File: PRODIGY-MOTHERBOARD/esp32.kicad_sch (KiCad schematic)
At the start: 14 parts, among them J15 Bus_M.2_Socket_B, J16 USB_C_Receptacle, J17 Conn_02x20_Odd_Even, SW2 SW_Push

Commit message: Finished v0.1 schematic.
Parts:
- added FID10, FID9: Fiducial, symbol Mechanical:Fiducial
- J6: renamed from J16; footprint (none) -> Connector_USB:USB_C_Receptacle_G-Switch_GT-USB-7025
- renumbered C57 to C26, D34 to D10, D31 to D11, D32 to D12, D33 to D13, D35 to D9, J15 to J7, J17 to J8, R34 to R19, R35 to R20, R32 to R21, R33 to R22
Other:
- moved on the sheet: J8

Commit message: MBT Schematic improved
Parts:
- J8: footprint Connector_PinHeader_2.54mm:PinHeader_2x20_P2.54mm_Horizontal -> Connector_IDC:IDC-Header_2x20_P2.54mm_Horizontal
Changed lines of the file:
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@@
 			)
 		)
-		(property "Footprint" "Connector_PinHeader_2.54mm:PinHeader_2x20_P2.54mm_Horizontal"
+		(property "Footprint" "Connector_IDC:IDC-Header_2x20_P2.54mm_Horizontal"
 			(at 238.76 119.38 0)
 			(effects

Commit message: schematic v0.2 finalized
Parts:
- added H10: MountingHole, MountingHole:MountingHole_3.2mm_M3_ISO7380_Pad_TopBottom, symbol Mechanical:MountingHole
- J8: now not fitted; now left out of the parts list
- renumbered C26 to C25
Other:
- note added: "In USB CDC Mode BOOT button is not needed"
- note removed: "In USB CDC Mode BOOT button is not needed, But externally accessible"
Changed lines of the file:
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@@
 		)
 	)
-	(text "In USB CDC Mode\nBOOT button is not needed,\nBut externally accessible"
+	(text "In USB CDC Mode\nBOOT button is not needed"
 		(exclude_from_sim no)
 		(at 109.22 190.754 0)
@@
 		(dnp no)
 		(fields_autoplaced yes)
-		(property "Reference" "#PWR052"
+		(property "Reference" "#PWR055"
 			(at 158.75 31.75 0)
 			(effects
@@
 			(project "PRODIGY-MOTHERBOARD"
 				(path "/f1c25860-8989-4190-bd24-2491d23ca7d9/4747deee-8806-443e-847a-65f550cadde4"
-					(reference "#PWR052")
+					(reference "#PWR055")
 					(unit 1)
 				)
@@
 		(dnp no)
 		(fields_autoplaced yes)
-		(property "Reference" "#PWR047"
+		(property "Reference" "#PWR050"
 			(at 44.45 189.23 0)
 			(effects
@@
 			(project "PRODIGY-MOTHERBOARD"
 				(path "/f1c25860-8989-4190-bd24-2491d23ca7d9/4747deee-8806-443e-847a-65f550cadde4"
-					(reference "#PWR047")
+					(reference "#PWR050")
 					(unit 1)
 				)
@@
 		(dnp no)
 		(fields_autoplaced yes)
-		(property "Reference" "#PWR054"
+		(property "Reference" "#PWR057"
 			(at 223.52 97.79 0)
 			(effects
@@
 			(project "PRODIGY-MOTHERBOARD"
 				(path "/f1c25860-8989-4190-bd24-2491d23ca7d9/4747deee-8806-443e-847a-65f550cadde4"
-					(reference "#PWR054")
+					(reference "#PWR057")
 					(unit 1)
 				)
@@
 		(dnp no)
 		(fields_autoplaced yes)
-		(property "Reference" "#PWR045"
+		(property "Reference" "#PWR048"
 			(at 38.1 157.48 0)
 			(effects
@@
 			(project "PRODIGY-MOTHERBOARD"
 				(path "/f1c25860-8989-4190-bd24-2491d23ca7d9/4747deee-8806-443e-847a-65f550cadde4"
-					(reference "#PWR045")
+					(reference "#PWR048")
 					(unit 1)
 				)
@@
 		(dnp no)
 		(fields_autoplaced yes)
-		(property "Reference" "C26"
+		(property "Reference" "C25"
 			(at 63.5 172.7199 0)
 			(effects
@@
 			(project "PRODIGY-MOTHERBOARD"
 				(path "/f1c25860-8989-4190-bd24-2491d23ca7d9/4747deee-8806-443e-847a-65f550cadde4"
-					(reference "C26")
+					(reference "C25")
 					(unit 1)
 				)
@@
 		(dnp no)
 		(fields_autoplaced yes)
-		(property "Reference" "#PWR049"
+		(property "Reference" "#PWR052"
 			(at 76.2 55.88 0)
 			(effects
@@
 			(project "PRODIGY-MOTHERBOARD"
 				(path "/f1c25860-8989-4190-bd24-2491d23ca7d9/4747deee-8806-443e-847a-65f550cadde4"
-					(reference "#PWR049")
+					(reference "#PWR052")
 					(unit 1)
 				)
@@
 		(dnp no)
 		(fields_autoplaced yes)
-		(property "Reference" "#PWR050"
+		(property "Reference" "#PWR053"
 			(at 85.09 92.71 0)
 			(effects
@@
 			(project "PRODIGY-MOTHERBOARD"
 				(path "/f1c25860-8989-4190-bd24-2491d23ca7d9/4747deee-8806-443e-847a-65f550cadde4"
-					(reference "#PWR050")
+					(reference "#PWR053")
 					(unit 1)
 				)
@@
 		(dnp no)
 		(fields_autoplaced yes)
-		(property "Reference" "#PWR048"
+		(property "Reference" "#PWR051"
 			(at 63.5 129.54 0)
 			(effects
@@
 			(project "PRODIGY-MOTHERBOARD"
 				(path "/f1c25860-8989-4190-bd24-2491d23ca7d9/4747deee-8806-443e-847a-65f550cadde4"
-					(reference "#PWR048")
+					(reference "#PWR051")
 					(unit 1)
 				)
@@
 		(dnp no)
 		(fields_autoplaced yes)
-		(property "Reference" "#PWR046"
+		(property "Reference" "#PWR049"
 			(at 40.64 130.81 0)
 			(effects
@@
 			(project "PRODIGY-MOTHERBOARD"
 				(path "/f1c25860-8989-4190-bd24-2491d23ca7d9/4747deee-8806-443e-847a-65f550cadde4"
-					(reference "#PWR046")
+					(reference "#PWR049")
 					(unit 1)
 				)
@@
 	)
 	(symbol
-		(lib_id "Connector_Generic:Conn_02x20_Odd_Even")
-		(at 238.76 119.38 0)
+		(lib_id "Mechanical:MountingHole")
+		(at 246.38 38.1 0)
 		(unit 1)
 		(exclude_from_sim no)
@@
 		(on_board yes)
 		(dnp no)
+		(fields_autoplaced yes)
+		(property "Reference" "H10"
+			(at 248.92 37.465 0)
+			(effects
+				(font
+					(size 1.27 1.27)
+				)
+				(justify left)
+			)
+		)
+		(property "Value" "MountingHole"
+			(at 248.92 40.005 0)
+			(effects
+				(font
+					(size 1.27 1.27)
+				)
+				(justify left)
+				(hide yes)
+			)
+		)
+		(property "Footprint" "MountingHole:MountingHole_3.2mm_M3_ISO7380_Pad_TopBottom"
+			(at 246.38 38.1 0)
+			(effects
+				(font
+					(size 1.27 1.27)
+				)
+				(hide yes)
+			)
+		)
+		(property "Datasheet" "~"
+			(at 246.38 38.1 0)
+			(effects
+				(font
+					(size 1.27 1.27)
+				)
+				(hide yes)
+			)
+		)
+		(property "Description" ""
+			(at 246.38 38.1 0)
+			(effects
+				(font
+					(size 1.27 1.27)
+				)
+				(hide yes)
+			)
+		)
+		(property "JLCPCB" ""
+			(at 246.38 38.1 0)
+			(effects
+				(font
+					(size 1.27 1.27)
+				)
+				(hide yes)
+			)
+		)
+		(instances
+			(project "PRODIGY-MOTHERBOARD"
+				(path "/f1c25860-8989-4190-bd24-2491d23ca7d9/4747deee-8806-443e-847a-65f550cadde4"
+					(reference "H10")
+					(unit 1)
+				)
+			)
+		)
+	)
+	(symbol
+		(lib_id "Connector_Generic:Conn_02x20_Odd_Even")
+		(at 238.76 119.38 0)
+		(unit 1)
+		(exclude_from_sim yes)
+		(in_bom no)
+		(on_board no)
+		(dnp yes)
 		(fields_autoplaced yes)
 		(property "Reference" "J8"
@@
 		(dnp no)
 		(fields_autoplaced yes)
-		(property "Reference" "#PWR056"
+		(property "Reference" "#PWR059"
 			(at 255.27 97.79 0)
 			(effects
@@
 			(project "PRODIGY-MOTHERBOARD"
 				(path "/f1c25860-8989-4190-bd24-2491d23ca7d9/4747deee-8806-443e-847a-65f550cadde4"
-					(reference "#PWR056")
+					(reference "#PWR059")
 					(unit 1)
 				)
@@
 		(dnp no)
 		(fields_autoplaced yes)
-		(property "Reference" "#PWR055"
+		(property "Reference" "#PWR058"
 			(at 227.33 153.67 0)
 			(effects
@@
 			(project "PRODIGY-MOTHERBOARD"
 				(path "/f1c25860-8989-4190-bd24-2491d23ca7d9/4747deee-8806-443e-847a-65f550cadde4"
-					(reference "#PWR055")
+					(reference "#PWR058")
 					(unit 1)
 				)
@@
 		(dnp no)
 		(fields_autoplaced yes)
-		(property "Reference" "#PWR051"
+		(property "Reference" "#PWR054"
 			(at 90.17 92.71 0)
 			(effects
@@
 			(project "PRODIGY-MOTHERBOARD"
 				(path "/f1c25860-8989-4190-bd24-2491d23ca7d9/4747deee-8806-443e-847a-65f550cadde4"
-					(reference "#PWR051")
+					(reference "#PWR054")
 					(unit 1)
 				)
@@
 		(dnp no)
 		(fields_autoplaced yes)
-		(property "Reference" "#PWR053"
+		(property "Reference" "#PWR056"
 			(at 158.75 137.16 0)
 			(effects
@@
 			(project "PRODIGY-MOTHERBOARD"
 				(path "/f1c25860-8989-4190-bd24-2491d23ca7d9/4747deee-8806-443e-847a-65f550cadde4"
-					(reference "#PWR053")
-					(unit 1)
-				)
+					(reference "#PWR056")
+					(unit 1)
+				)

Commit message: ESP32 schematic complete.
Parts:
- H10: footprint MountingHole:MountingHole_3.2mm_M3_ISO7380_Pad_TopBottom -> MountingHole:MountingHole_4.3mm_M4_ISO14580_Pad
- J7: footprint (none) -> m.2_edge_connector_key_a:121992304
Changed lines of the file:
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@@
 			)
 		)
-		(property "Footprint" "MountingHole:MountingHole_3.2mm_M3_ISO7380_Pad_TopBottom"
+		(property "Footprint" "MountingHole:MountingHole_4.3mm_M4_ISO14580_Pad"
 			(at 246.38 38.1 0)
 			(effects
@@
 			)
 		)
-		(property "Footprint" ""
+		(property "Footprint" "m.2_edge_connector_key_a:121992304"
 			(at 158.75 53.34 0)
 			(effects

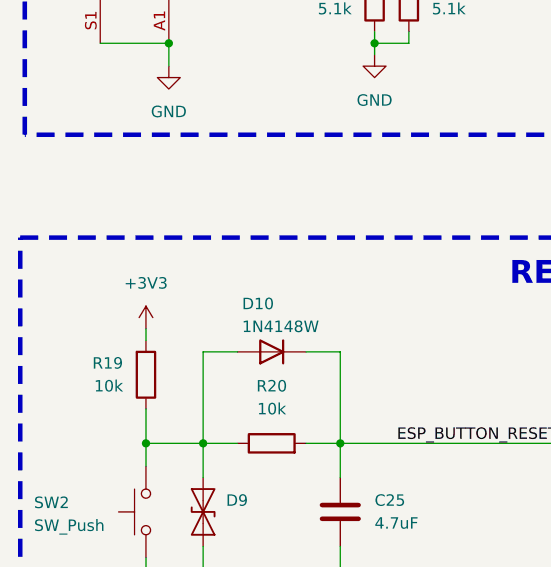
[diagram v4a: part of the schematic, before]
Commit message: Motherboard footprints assigned.
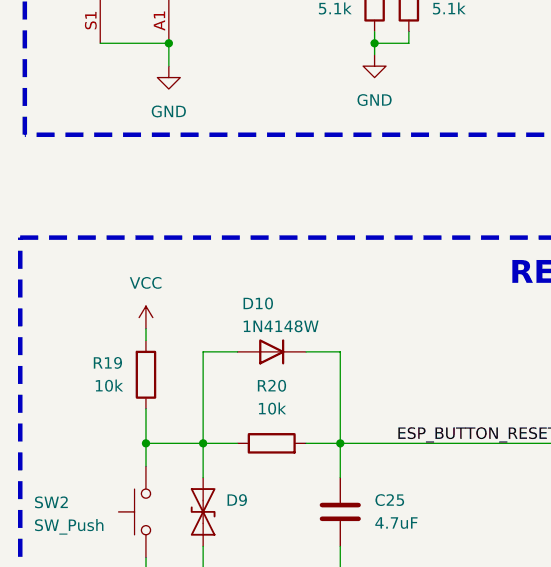
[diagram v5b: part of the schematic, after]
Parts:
- C25: footprint (none) -> Capacitor_SMD:C_0805_2012Metric
- FID10, FID9: footprint (none) -> Fiducial:Fiducial_1mm_Mask3mm
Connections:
- net +3V3: no longer R19.2
- new net VCC: R19.2

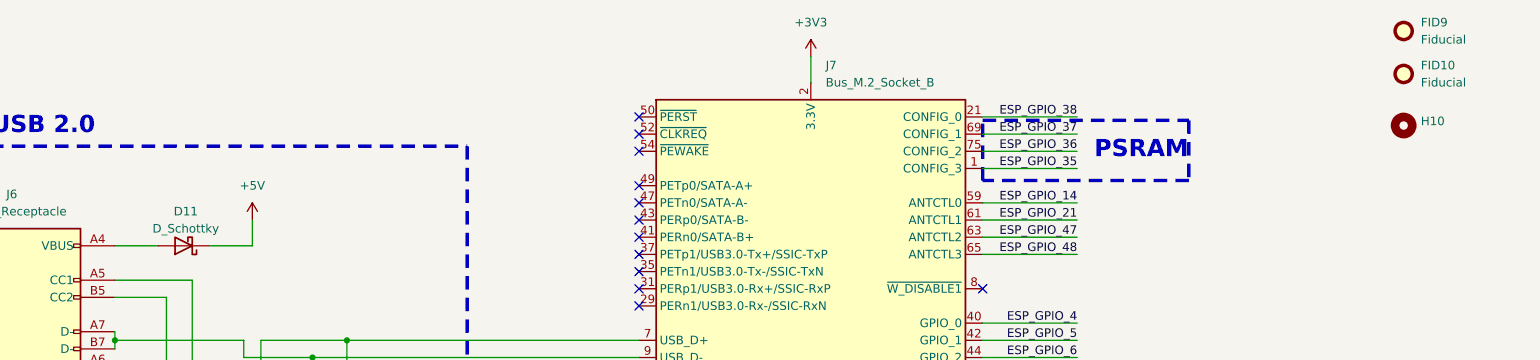
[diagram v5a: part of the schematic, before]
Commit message: finished motherboard bom and updated footprints
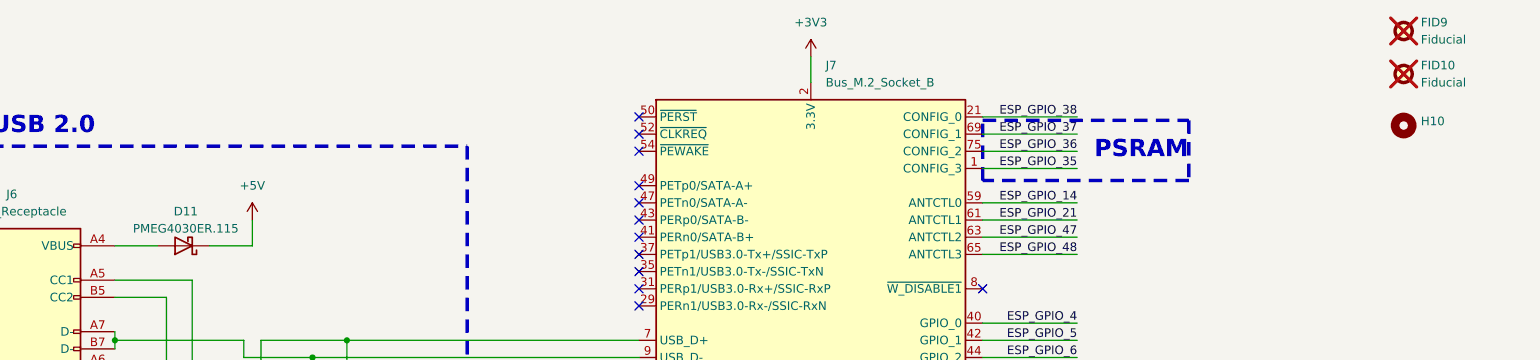
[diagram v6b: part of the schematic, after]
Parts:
- C25: TME (none) -> CL21A475KAQNNNG
- D10: footprint Diode_SMD:D_SOD-123 -> Diode_SMD:D_SOD-323; TME (none) -> 1N4148WSTR-SMC
- D11: value D_Schottky -> PMEG4030ER.115; footprint Diode_SMD:D_SMB -> Diode_SMD:Nexperia_CFP3_SOD-123W; TME (none) -> PMEG4030ER.115
- D12, D13, D9: TME (none) -> SD05.TCT
- FID10, FID9: now not fitted
- H10: MOUSER (none) -> 710-9774040360R
- J6: MOUSER (none) -> 523-GSB1C411111DS1HR
- J7: TME (none) -> 123A-58B00
- R19, R20: TME (none) -> WR06X1002FTL
- R21, R22: TME (none) -> AC0603FR-075K1L
- SW2: TME (none) -> KMR231GLFS
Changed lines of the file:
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@@
 			)
 		)
-		(property "TME" ""
+		(property "TME" "AC0603FR-075K1L"
 			(at 63.5 116.84 0)
 			(effects
@@
 			)
 		)
-		(property "TME" ""
+		(property "TME" "SD05.TCT "
 			(at 90.17 80.01 0)
 			(effects
@@
 			)
 		)
-		(property "MOUSER" ""
+		(property "MOUSER" " 523-GSB1C411111DS1HR "
 			(at 40.64 81.28 0)
 			(effects
@@
 			)
 		)
-		(property "TME" ""
+		(property "TME" "KMR231GLFS "
 			(at 38.1 173.99 0)
 			(effects
@@
 			)
 		)
-		(property "TME" ""
+		(property "TME" "SD05.TCT "
 			(at 44.45 173.99 0)
 			(effects
@@
 			)
 		)
-		(property "TME" ""
+		(property "TME" "SD05.TCT "
 			(at 85.09 80.01 0)
 			(effects
@@
 		(in_bom yes)
 		(on_board yes)
-		(dnp no)
+		(dnp yes)
 		(fields_autoplaced yes)
 		(property "Reference" "FID9"
@@
 			)
 		)
-		(property "TME" ""
+		(property "TME" "CL21A475KAQNNNG"
 			(at 59.69 173.99 0)
 			(effects
@@
 			)
 		)
-		(property "TME" ""
+		(property "TME" "WR06X1002FTL "
 			(at 52.07 166.37 0)
 			(effects
@@
 			)
 		)
-		(property "TME" ""
+		(property "TME" "AC0603FR-075K1L"
 			(at 67.31 116.84 0)
 			(effects
@@
 		(in_bom yes)
 		(on_board yes)
-		(dnp no)
+		(dnp yes)
 		(fields_autoplaced yes)
 		(property "Reference" "FID10"
@@
 			)
 		)
-		(property "TME" ""
+		(property "TME" "WR06X1002FTL "
 			(at 38.1 158.75 0)
 			(effects
@@
 			)
 		)
-		(property "MOUSER" ""
+		(property "MOUSER" " 710-9774040360R "
 			(at 246.38 38.1 0)
 			(effects
@@
 			)
 		)
-		(property "Footprint" "Diode_SMD:D_SOD-123"
+		(property "Footprint" "Diode_SMD:D_SOD-323"
 			(at 52.07 151.765 0)
 			(effects
@@
 			)
 		)
-		(property "TME" ""
+		(property "TME" "1N4148WSTR-SMC"
 			(at 52.07 156.21 0)
 			(effects
@@
 			)
 		)
-		(property "Value" "D_Schottky"
+		(property "Value" "PMEG4030ER.115"
 			(at 66.3575 53.34 0)
 			(effects
@@
 			)
 		)
-		(property "Footprint" "Diode_SMD:D_SMB"
+		(property "Footprint" "Diode_SMD:Nexperia_CFP3_SOD-123W"
 			(at 66.04 55.88 0)
 			(effects
@@
 			)
 		)
-		(property "TME" ""
+		(property "TME" "PMEG4030ER.115"
 			(at 66.04 55.88 0)
 			(effects
@@
 			)
 		)
-		(property "TME" ""
+		(property "TME" "123A-58B00"
 			(at 158.75 80.01 0)
 			(effects

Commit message: Motherboard PCB layout started
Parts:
- J6: footprint Connector_USB:USB_C_Receptacle_G-Switch_GT-USB-7025 -> Connector_USB:USB_C_Receptacle_XKB_U262-16XN-4BVC11
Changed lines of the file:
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@@
 			)
 		)
-		(property "Footprint" "Connector_USB:USB_C_Receptacle_G-Switch_GT-USB-7025"
+		(property "Footprint" "Connector_USB:USB_C_Receptacle_XKB_U262-16XN-4BVC11"
 			(at 44.45 81.28 0)
 			(effects
@@
 		)
 		(instances
-			(project ""
+			(project "PRODIGY-MOTHERBOARD"
 				(path "/f1c25860-8989-4190-bd24-2491d23ca7d9/4747deee-8806-443e-847a-65f550cadde4"
 					(reference "FID9")

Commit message: Analog lazout done
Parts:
- removed FID10, FID9: Fiducial, Fiducial:Fiducial_1mm_Mask3mm, symbol Mechanical:Fiducial
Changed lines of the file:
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@@
-	)
-	(symbol
-		(lib_id "Mechanical:Fiducial")
-		(at 246.38 24.13 0)
-		(unit 1)
-		(exclude_from_sim no)
-		(in_bom yes)
-		(on_board yes)
-		(dnp yes)
-		(fields_autoplaced yes)
-		(property "Reference" "FID9"
-			(at 248.92 22.8599 0)
-			(effects
-				(font
-					(size 1.27 1.27)
-				)
-				(justify left)
-			)
-		)
-		(property "Value" "Fiducial"
-			(at 248.92 25.3999 0)
-			(effects
-				(font
-					(size 1.27 1.27)
-				)
-				(justify left)
-			)
-		)
-		(property "Footprint" "Fiducial:Fiducial_1mm_Mask3mm"
-			(at 246.38 24.13 0)
-			(effects
-				(font
-					(size 1.27 1.27)
-				)
-				(hide yes)
-			)
-		)
-		(property "Datasheet" "~"
-			(at 246.38 24.13 0)
-			(effects
-				(font
-					(size 1.27 1.27)
-				)
-				(hide yes)
-			)
-		)
-		(property "Description" "Fiducial Marker"
-			(at 246.38 24.13 0)
-			(effects
-				(font
-					(size 1.27 1.27)
-				)
-				(hide yes)
-			)
-		)
-		(property "MOUSER" ""
-			(at 246.38 24.13 0)
-			(effects
-				(font
-					(size 1.27 1.27)
-				)
-				(hide yes)
-			)
-		)
-		(property "Sim.Type" ""
-			(at 246.38 24.13 0)
-			(effects
-				(font
-					(size 1.27 1.27)
-				)
-				(hide yes)
-			)
-		)
-		(property "TME" ""
-			(at 246.38 24.13 0)
-			(effects
-				(font
-					(size 1.27 1.27)
-				)
-				(hide yes)
-			)
-		)
-		(instances
-			(project "PRODIGY-MOTHERBOARD"
-				(path "/f1c25860-8989-4190-bd24-2491d23ca7d9/4747deee-8806-443e-847a-65f550cadde4"
-					(reference "FID9")
-					(unit 1)
-				)
-			)
-		)
 	)
 	(symbol
@@
 					(unit 1)
 				)
-			)
-		)
-	)
-	(symbol
-		(lib_id "Mechanical:Fiducial")
-		(at 246.38 30.48 0)
-		(unit 1)
-		(exclude_from_sim no)
-		(in_bom yes)
-		(on_board yes)
-		(dnp yes)
-		(fields_autoplaced yes)
-		(property "Reference" "FID10"
-			(at 248.92 29.2099 0)
-			(effects
-				(font
-					(size 1.27 1.27)
-				)
-				(justify left)
-			)
-		)
-		(property "Value" "Fiducial"
-			(at 248.92 31.7499 0)
-			(effects
-				(font
-					(size 1.27 1.27)
-				)
-				(justify left)
-			)
-		)
-		(property "Footprint" "Fiducial:Fiducial_1mm_Mask3mm"
-			(at 246.38 30.48 0)
-			(effects
-				(font
-					(size 1.27 1.27)
-				)
-				(hide yes)
-			)
-		)
-		(property "Datasheet" "~"
-			(at 246.38 30.48 0)
-			(effects
-				(font
-					(size 1.27 1.27)
-				)
-				(hide yes)
-			)
-		)
-		(property "Description" "Fiducial Marker"
-			(at 246.38 30.48 0)
-			(effects
-				(font
-					(size 1.27 1.27)
-				)
-				(hide yes)
-			)
-		)
-		(property "MOUSER" ""
-			(at 246.38 30.48 0)
-			(effects
-				(font
-					(size 1.27 1.27)
-				)
-				(hide yes)
-			)
-		)
-		(property "Sim.Type" ""
-			(at 246.38 30.48 0)
-			(effects
-				(font
-					(size 1.27 1.27)
-				)
-				(hide yes)
-			)
-		)
-		(property "TME" ""
-			(at 246.38 30.48 0)
-			(effects
-				(font
-					(size 1.27 1.27)
-				)
-				(hide yes)
-			)
-		)
-		(instances
-			(project "PRODIGY-MOTHERBOARD"
-				(path "/f1c25860-8989-4190-bd24-2491d23ca7d9/4747deee-8806-443e-847a-65f550cadde4"
-					(reference "FID10")
-					(unit 1)
-				)
